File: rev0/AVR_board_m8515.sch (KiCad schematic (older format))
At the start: 8 parts

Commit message: added all needed labels and stuff
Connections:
- net VCC: now also P?.1 (P1)
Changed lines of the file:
@@
 LIBS:contrib
 LIBS:valves
+LIBS:AVR_board_m8515-cache
 EELAYER 24 0
 EELAYER END
@@
 Wire Wire Line
 	7350 3850 7350 3950
+$Comp
+L VCC #PWR?
+U 1 1 54189251
+P 6600 800
+F 0 "#PWR?" H 6600 900 30  0001 C CNN
+F 1 "VCC" H 6600 900 30  0000 C CNN
+F 2 "" H 6600 800 60  0000 C CNN
+F 3 "" H 6600 800 60  0000 C CNN
+	1    6600 800
+	1    0    0    -1
+$EndComp
+Wire Wire Line
+	6600 800  6600 1000
+Wire Wire Line
+	6600 1000 6700 1000
+Text GLabel 6500 1100 0    60   Input ~ 0
+PA0
+Text GLabel 6500 1200 0    60   Input ~ 0
+PA1
+Text GLabel 6500 1300 0    60   Input ~ 0
+PA2
+Text GLabel 6500 1400 0    60   Input ~ 0
+PA3
+Text GLabel 6500 1500 0    60   Input ~ 0
+PA4
+Text GLabel 6500 1600 0    60   Input ~ 0
+PA5
+Text GLabel 6500 1700 0    60   Input ~ 0
+PA6
+Text GLabel 6500 1800 0    60   Input ~ 0
+PA7
+Text GLabel 6500 1900 0    60   Input ~ 0
+PE0
+Text GLabel 6500 2000 0    60   Input ~ 0
+PE1
+Text GLabel 6500 2100 0    60   Input ~ 0
+PE2
+Text GLabel 6500 2200 0    60   Input ~ 0
+PC7
+Text GLabel 6500 2300 0    60   Input ~ 0
+PC6
+Text GLabel 6500 2400 0    60   Input ~ 0
+PC5
+Text GLabel 6500 2500 0    60   Input ~ 0
+PC4
+Text GLabel 6500 2600 0    60   Input ~ 0
+PC3
+Text GLabel 6500 2700 0    60   Input ~ 0
+PC2
+Text GLabel 6500 2800 0    60   Input ~ 0
+PC1
+Text GLabel 6500 2900 0    60   Input ~ 0
+PC0
+Text GLabel 3800 1000 2    60   Input ~ 0
+PB0
+Text GLabel 3800 1100 2    60   Input ~ 0
+PB1
+Text GLabel 3800 1200 2    60   Input ~ 0
+PB2
+Text GLabel 3800 1300 2    60   Input ~ 0
+PB3
+Text GLabel 3800 1400 2    60   Input ~ 0
+PB4
+Text GLabel 3800 1500 2    60   Input ~ 0
+PB5
+Text GLabel 3800 1600 2    60   Input ~ 0
+PB6
+Text GLabel 3800 1700 2    60   Input ~ 0
+PB7
+Text GLabel 3800 1800 2    60   Input ~ 0
+RESET
+Text GLabel 3800 1900 2    60   Input ~ 0
+PD0
+Text GLabel 3800 2000 2    60   Input ~ 0
+PD1
+Text GLabel 3800 2100 2    60   Input ~ 0
+PD2
+Text GLabel 3800 2200 2    60   Input ~ 0
+PD3
+Text GLabel 3800 2300 2    60   Input ~ 0
+PD4
+Text GLabel 3800 2400 2    60   Input ~ 0
+PD5
+Text GLabel 3800 2500 2    60   Input ~ 0
+PD6
+Text GLabel 3800 2600 2    60   Input ~ 0
+PD7
+Text GLabel 3800 2700 2    60   Input ~ 0
+XTAL2
+Text GLabel 3800 2800 2    60   Input ~ 0
+XTAL1
+Text GLabel 3800 2900 2    60   Input ~ 0
+GND
 $EndSCHEMATC

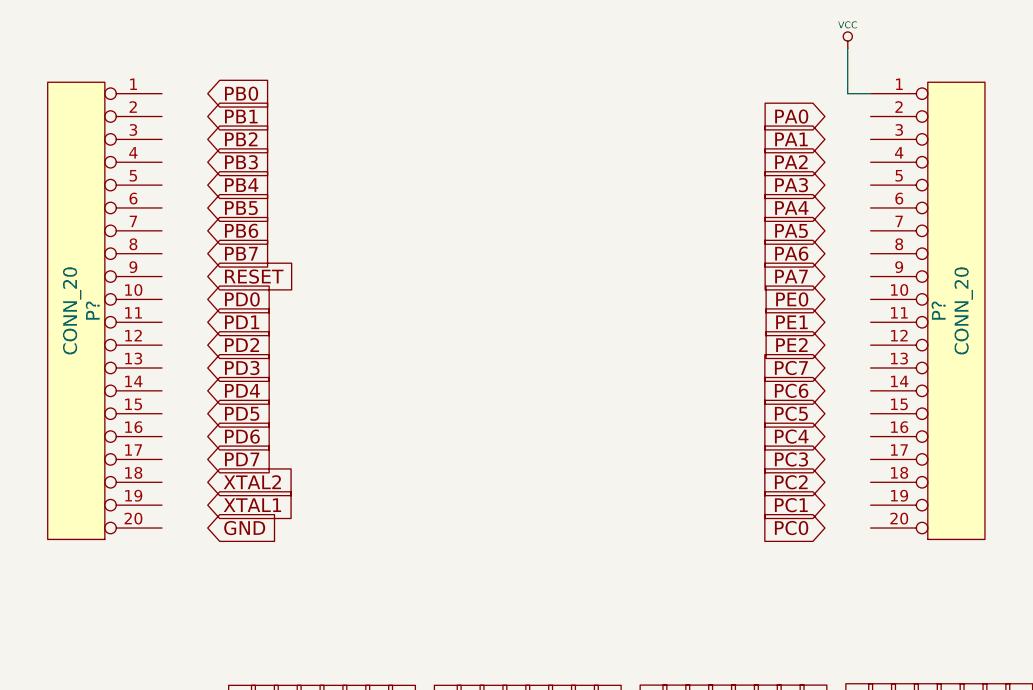
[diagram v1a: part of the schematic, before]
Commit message: added connections to the labels
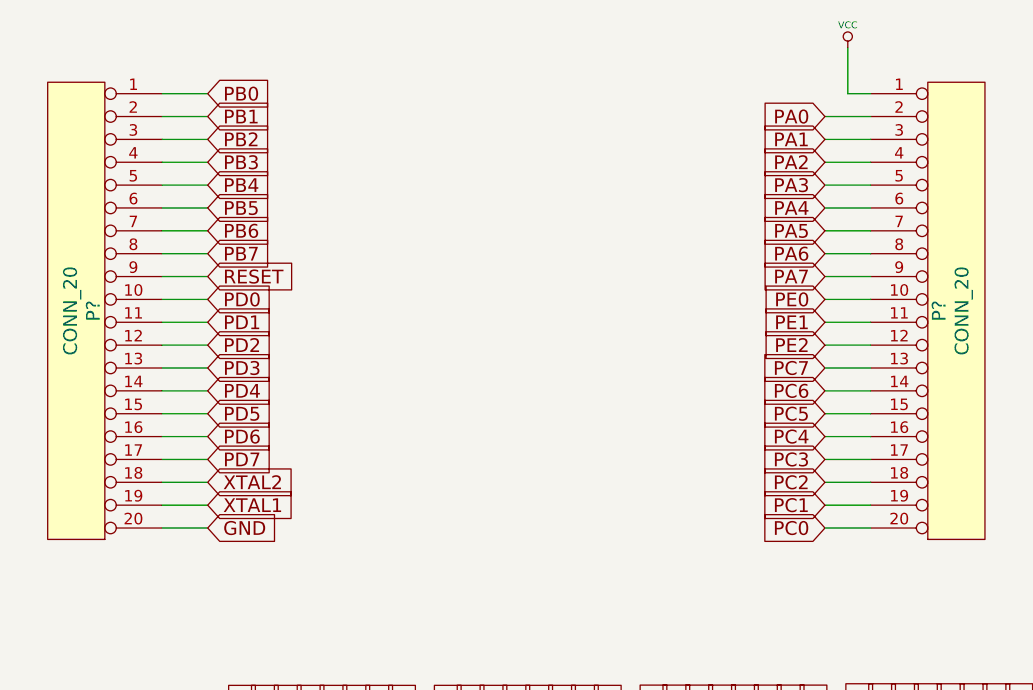
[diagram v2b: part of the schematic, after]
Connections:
- net GND: now also P?.20 (P20)
- net PA0: now also P?.2 (P2)
- net PA1: now also P?.3 (P3)
- net PA2: now also P?.4 (P4)
- net PA3: now also P?.5 (P5)
- net PA4: now also P?.6 (P6)
- net PA5: now also P?.7 (P7)
- net PA6: now also P?.8 (P8)
- net PA7: now also P?.9 (P9)
- net PB0: now also P?.1 (P1)
- net PB1: now also P?.2 (P2)
- net PB2: now also P?.3 (P3)
- net PB3: now also P?.4 (P4)
- net PB4: now also P?.5 (P5)
- net PB5: now also P?.6 (P6)
- net PB6: now also P?.7 (P7)
- net PB7: now also P?.8 (P8)
- net PC0: now also P?.20 (P20)
- net PC1: now also P?.19 (P19)
- net PC2: now also P?.18 (P18)
- net PC3: now also P?.17 (P17)
- net PC4: now also P?.16 (P16)
- net PC5: now also P?.15 (P15)
- net PC6: now also P?.14 (P14)
- net PC7: now also P?.13 (P13)
- net PD0: now also P?.10 (P10)
- net PD1: now also P?.11 (P11)
- net PD2: now also P?.12 (P12)
- net PD3: now also P?.13 (P13)
- net PD4: now also P?.14 (P14)
- net PD5: now also P?.15 (P15)
- net PD6: now also P?.16 (P16)
- net PD7: now also P?.17 (P17)
- net PE0: now also P?.10 (P10)
- net PE1: now also P?.11 (P11)
- net PE2: now also P?.12 (P12)
- net RESET: now also P?.9 (P9)
- net XTAL1: now also P?.19 (P19)
- net XTAL2: now also P?.18 (P18)
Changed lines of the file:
@@
 Text GLabel 3800 2900 2    60   Input ~ 0
 GND
+Wire Wire Line
+	3800 1000 3600 1000
+Wire Wire Line
+	3800 1100 3600 1100
+Wire Wire Line
+	3800 1200 3600 1200
+Wire Wire Line
+	3800 1300 3600 1300
+Wire Wire Line
+	3800 1400 3600 1400
+Wire Wire Line
+	3800 1500 3600 1500
+Wire Wire Line
+	3800 1600 3600 1600
+Wire Wire Line
+	3800 1700 3600 1700
+Wire Wire Line
+	3800 1800 3600 1800
+Wire Wire Line
+	3800 1900 3600 1900
+Wire Wire Line
+	3800 2000 3600 2000
+Wire Wire Line
+	3800 2100 3600 2100
+Wire Wire Line
+	3800 2200 3600 2200
+Wire Wire Line
+	3800 2300 3600 2300
+Wire Wire Line
+	3600 2400 3800 2400
+Wire Wire Line
+	3800 2500 3600 2500
+Wire Wire Line
+	3800 2600 3600 2600
+Wire Wire Line
+	3800 2700 3600 2700
+Wire Wire Line
+	3800 2800 3600 2800
+Wire Wire Line
+	3800 2900 3600 2900
+Wire Wire Line
+	6500 1100 6700 1100
+Wire Wire Line
+	6700 1200 6500 1200
+Wire Wire Line
+	6500 1300 6700 1300
+Wire Wire Line
+	6700 1400 6500 1400
+Wire Wire Line
+	6700 1500 6500 1500
+Wire Wire Line
+	6700 1600 6500 1600
+Wire Wire Line
+	6700 1700 6500 1700
+Wire Wire Line
+	6700 1800 6500 1800
+Wire Wire Line
+	6700 1900 6500 1900
+Wire Wire Line
+	6700 2000 6500 2000
+Wire Wire Line
+	6700 2100 6500 2100
+Wire Wire Line
+	6700 2200 6500 2200
+Wire Wire Line
+	6700 2300 6500 2300
+Wire Wire Line
+	6700 2400 6500 2400
+Wire Wire Line
+	6700 2500 6500 2500
+Wire Wire Line
+	6700 2600 6500 2600
+Wire Wire Line
+	6500 2700 6700 2700
+Wire Wire Line
+	6700 2800 6500 2800
+Wire Wire Line
+	6500 2900 6700 2900
 $EndSCHEMATC

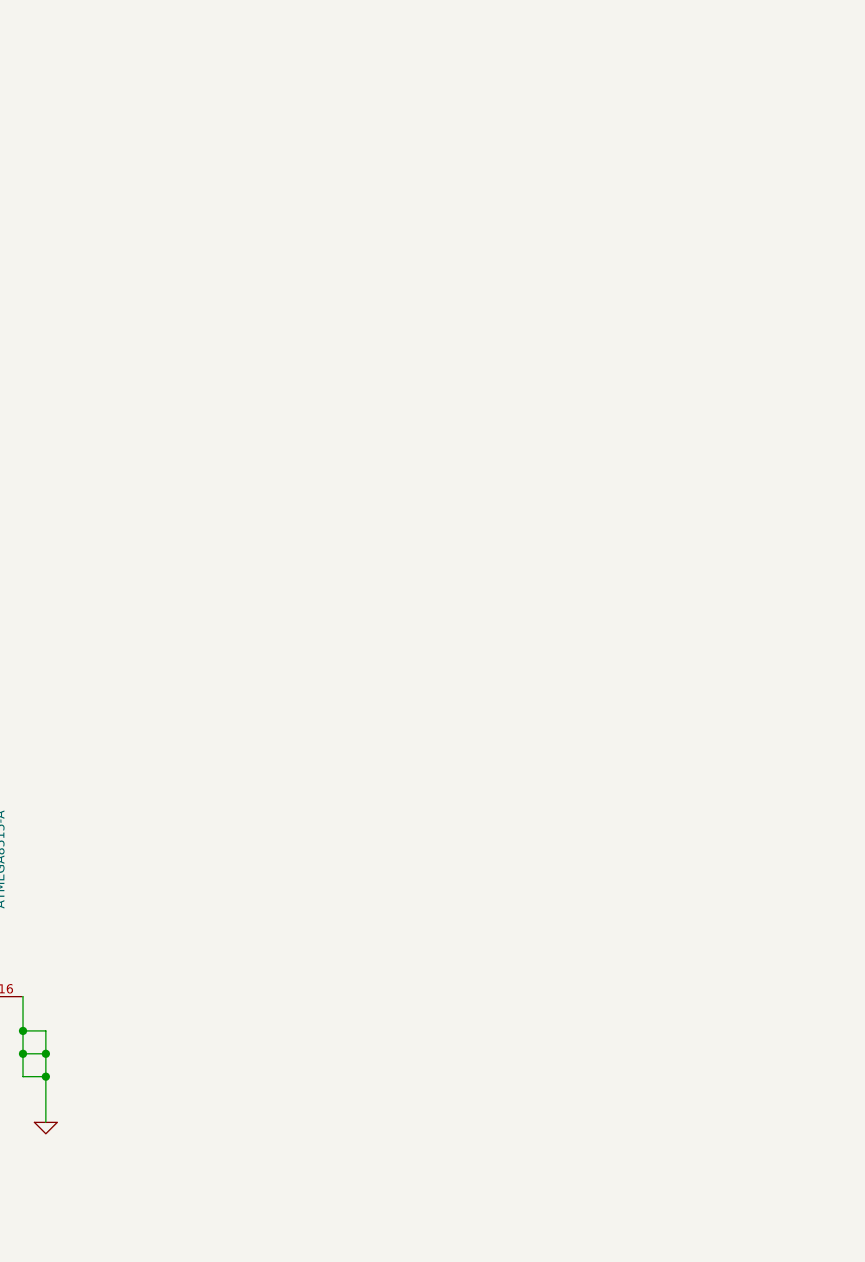
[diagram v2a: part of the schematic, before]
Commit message: added wires to the things to other mcu pad placeholder thingy
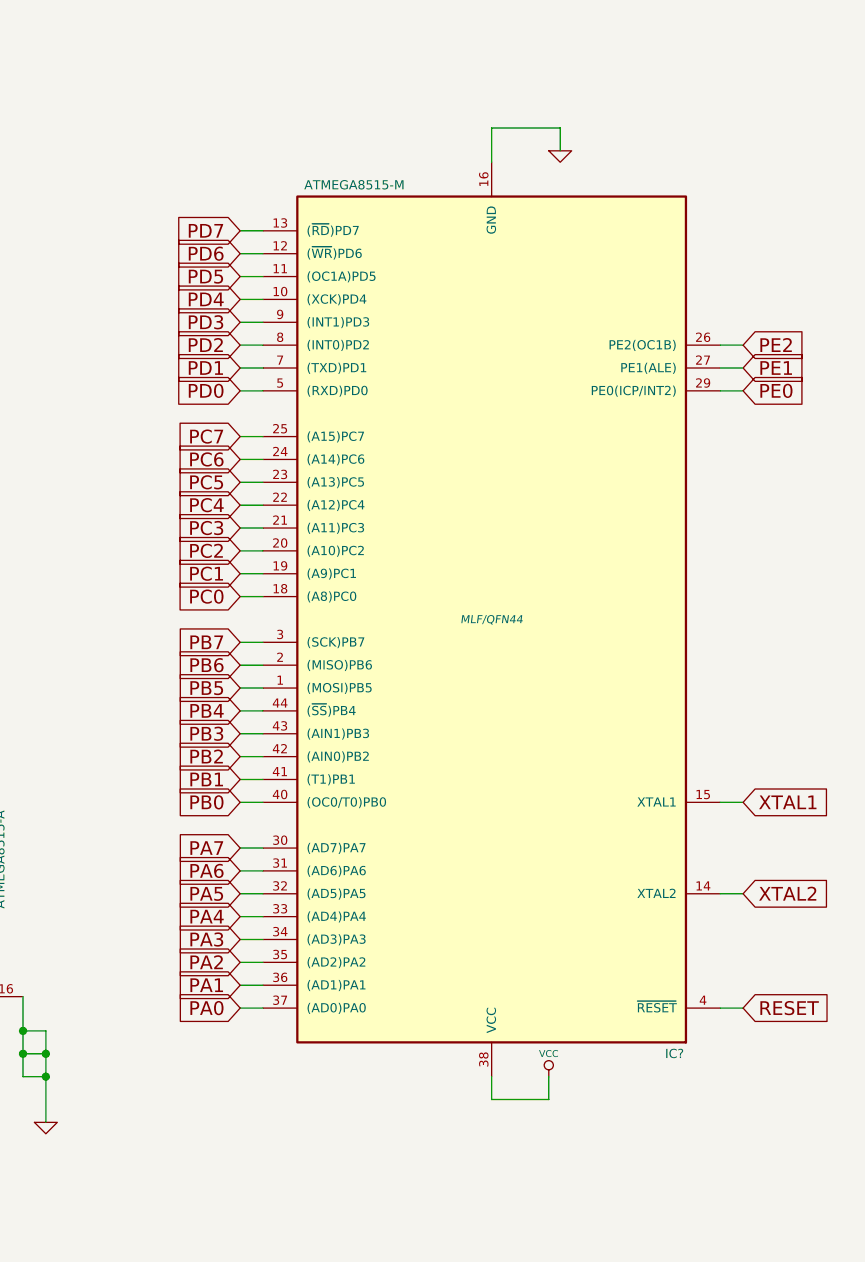
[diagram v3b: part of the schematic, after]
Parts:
- added IC?: ATMEGA8515-M, MLF/QFN44, symbol ATMEGA8515-M
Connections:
- net GND: now also IC?.16 (GND)
- net PA0: now also IC?.37 ((AD0)PA0)
- net PA1: now also IC?.36 ((AD1)PA1)
- net PA2: now also IC?.35 ((AD2)PA2)
- net PA3: now also IC?.34 ((AD3)PA3)
- net PA4: now also IC?.33 ((AD4)PA4)
- net PA5: now also IC?.32 ((AD5)PA5)
- net PA6: now also IC?.31 ((AD6)PA6)
- net PA7: now also IC?.30 ((AD7)PA7)
- net PB0: now also IC?.40 ((OC0/T0)PB0)
- net PB1: now also IC?.41 ((T1)PB1)
- net PB2: now also IC?.42 ((AIN0)PB2)
- net PB3: now also IC?.43 ((AIN1)PB3)
- net PB4: now also IC?.44 ((~SS~)PB4)
- net PB5: now also IC?.1 ((MOSI)PB5)
- net PB6: now also IC?.2 ((MISO)PB6)
- net PB7: now also IC?.3 ((SCK)PB7)
- net PC0: now also IC?.18 ((A8)PC0)
- net PC1: now also IC?.19 ((A9)PC1)
- net PC2: now also IC?.20 ((A10)PC2)
- net PC3: now also IC?.21 ((A11)PC3)
- net PC4: now also IC?.22 ((A12)PC4)
- net PC5: now also IC?.23 ((A13)PC5)
- net PC6: now also IC?.24 ((A14)PC6)
- net PC7: now also IC?.25 ((A15)PC7)
- net PD0: now also IC?.5 ((RXD)PD0)
- net PD1: now also IC?.7 ((TXD)PD1)
- net PD2: now also IC?.8 ((INT0)PD2)
- net PD3: now also IC?.9 ((INT1)PD3)
- net PD4: now also IC?.10 ((XCK)PD4)
- net PD5: now also IC?.11 ((OC1A)PD5)
- net PD6: now also IC?.12 ((~WR~)PD6)
- net PD7: now also IC?.13 ((~RD~)PD7)
- net PE0: now also IC?.29 (PE0(ICP/INT2))
- net PE1: now also IC?.27 (PE1(ALE))
- net PE2: now also IC?.26 (PE2(OC1B))
- net RESET: now also IC?.4 (~RESET)
- net VCC: now also IC?.38 (VCC)
- net XTAL1: now also IC?.15 (XTAL1)
- net XTAL2: now also IC?.14 (XTAL2)
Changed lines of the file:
@@
 Wire Wire Line
 	6500 2900 6700 2900
+$Comp
+L ATMEGA8515-M IC?
+U 1 1 5418A671
+P 9700 3300
+F 0 "IC?" H 8900 5200 40  0000 C CNN
+F 1 "ATMEGA8515-M" H 10300 1400 40  0000 C CNN
+F 2 "MLF/QFN44" H 9700 3300 35  0000 C CIN
+F 3 "" H 9700 3300 60  0000 C CNN
+	1    9700 3300
+	-1   0    0    1
+$EndComp
+$Comp
+L GND #PWR?
+U 1 1 5418A680
+P 10000 1250
+F 0 "#PWR?" H 10000 1250 30  0001 C CNN
+F 1 "GND" H 10000 1180 30  0001 C CNN
+F 2 "" H 10000 1250 60  0000 C CNN
+F 3 "" H 10000 1250 60  0000 C CNN
+	1    10000 1250
+	1    0    0    -1
+$EndComp
+Wire Wire Line
+	9700 1300 9700 1150
+Wire Wire Line
+	9700 1150 10000 1150
+Wire Wire Line
+	10000 1150 10000 1250
+Text GLabel 8600 1600 0    60   Input ~ 0
+PD7
+Text GLabel 8600 1700 0    60   Input ~ 0
+PD6
+Text GLabel 8600 1800 0    60   Input ~ 0
+PD5
+Text GLabel 8600 1900 0    60   Input ~ 0
+PD4
+Text GLabel 8600 2000 0    60   Input ~ 0
+PD3
+Text GLabel 8600 2100 0    60   Input ~ 0
+PD2
+Text GLabel 8600 2200 0    60   Input ~ 0
+PD1
+Text GLabel 8600 2300 0    60   Input ~ 0
+PD0
+Text GLabel 8600 2500 0    60   Input ~ 0
+PC7
+Text GLabel 8600 2600 0    60   Input ~ 0
+PC6
+Text GLabel 8600 2700 0    60   Input ~ 0
+PC5
+Text GLabel 8600 2800 0    60   Input ~ 0
+PC4
+Text GLabel 8600 2900 0    60   Input ~ 0
+PC3
+Text GLabel 8600 3000 0    60   Input ~ 0
+PC2
+Text GLabel 8600 3100 0    60   Input ~ 0
+PC1
+Text GLabel 8600 3200 0    60   Input ~ 0
+PC0
+Text GLabel 8600 3400 0    60   Input ~ 0
+PB7
+Text GLabel 8600 3500 0    60   Input ~ 0
+PB6
+Text GLabel 8600 3600 0    60   Input ~ 0
+PB5
+Text GLabel 8600 3700 0    60   Input ~ 0
+PB4
+Text GLabel 8600 3800 0    60   Input ~ 0
+PB3
+Text GLabel 8600 3900 0    60   Input ~ 0
+PB2
+Text GLabel 8600 4000 0    60   Input ~ 0
+PB1
+Text GLabel 8600 4100 0    60   Input ~ 0
+PB0
+Text GLabel 8600 4300 0    60   Input ~ 0
+PA7
+Text GLabel 8600 4400 0    60   Input ~ 0
+PA6
+Text GLabel 8600 4500 0    60   Input ~ 0
+PA5
+Text GLabel 8600 4600 0    60   Input ~ 0
+PA4
+Text GLabel 8600 4700 0    60   Input ~ 0
+PA3
+Text GLabel 8600 4800 0    60   Input ~ 0
+PA2
+Text GLabel 8600 4900 0    60   Input ~ 0
+PA1
+Text GLabel 8600 5000 0    60   Input ~ 0
+PA0
+$Comp
+L VCC #PWR?
+U 1 1 5418A7C7
+P 9950 5300
+F 0 "#PWR?" H 9950 5400 30  0001 C CNN
+F 1 "VCC" H 9950 5400 30  0000 C CNN
+F 2 "" H 9950 5300 60  0000 C CNN
+F 3 "" H 9950 5300 60  0000 C CNN
+	1    9950 5300
+	1    0    0    -1
+$EndComp
+Wire Wire Line
+	9700 5300 9700 5400
+Wire Wire Line
+	9700 5400 9950 5400
+Wire Wire Line
+	9950 5400 9950 5300
+Text GLabel 10800 5000 2    60   Input ~ 0
+RESET
+Text GLabel 10800 4500 2    60   Input ~ 0
+XTAL2
+Text GLabel 10800 4100 2    60   Input ~ 0
+XTAL1
+Text GLabel 10800 2300 2    60   Input ~ 0
+PE0
+Text GLabel 10800 2200 2    60   Input ~ 0
+PE1
+Text GLabel 10800 2100 2    60   Input ~ 0
+PE2
+Wire Wire Line
+	10800 4100 10700 4100
+Wire Wire Line
+	10800 4500 10700 4500
+Wire Wire Line
+	10800 5000 10700 5000
+Wire Wire Line
+	10800 2100 10700 2100
+Wire Wire Line
+	10800 2200 10700 2200
+Wire Wire Line
+	10800 2300 10700 2300
+Wire Wire Line
+	8600 1600 8700 1600
+Wire Wire Line
+	8600 1700 8700 1700
+Wire Wire Line
+	8700 1800 8600 1800
+Wire Wire Line
+	8600 1900 8700 1900
+Wire Wire Line
+	8700 2000 8600 2000
+Wire Wire Line
+	8700 2100 8600 2100
+Wire Wire Line
+	8700 2200 8600 2200
+Wire Wire Line
+	8700 2300 8600 2300
+Wire Wire Line
+	8700 2500 8600 2500
+Wire Wire Line
+	8700 2600 8600 2600
+Wire Wire Line
+	8700 2700 8600 2700
+Wire Wire Line
+	8700 2800 8600 2800
+Wire Wire Line
+	8700 2900 8600 2900
+Wire Wire Line
+	8700 3000 8600 3000
+Wire Wire Line
+	8700 3100 8600 3100
+Wire Wire Line
+	8700 3200 8600 3200
+Wire Wire Line
+	8700 3400 8600 3400
+Wire Wire Line
+	8700 3500 8600 3500
+Wire Wire Line
+	8700 3600 8600 3600
+Wire Wire Line
+	8700 3700 8600 3700
+Wire Wire Line
+	8700 3800 8600 3800
+Wire Wire Line
+	8700 3900 8600 3900
+Wire Wire Line
+	8700 4000 8600 4000
+Wire Wire Line
+	8700 4100 8600 4100
+Wire Wire Line
+	8700 4300 8600 4300
+Wire Wire Line
+	8700 4400 8600 4400
+Wire Wire Line
+	8700 4500 8600 4500
+Wire Wire Line
+	8700 4600 8600 4600
+Wire Wire Line
+	8700 4700 8600 4700
+Wire Wire Line
+	8700 4800 8600 4800
+Wire Wire Line
+	8700 4900 8600 4900
+Wire Wire Line
+	8700 5000 8600 5000
 $EndSCHEMATC

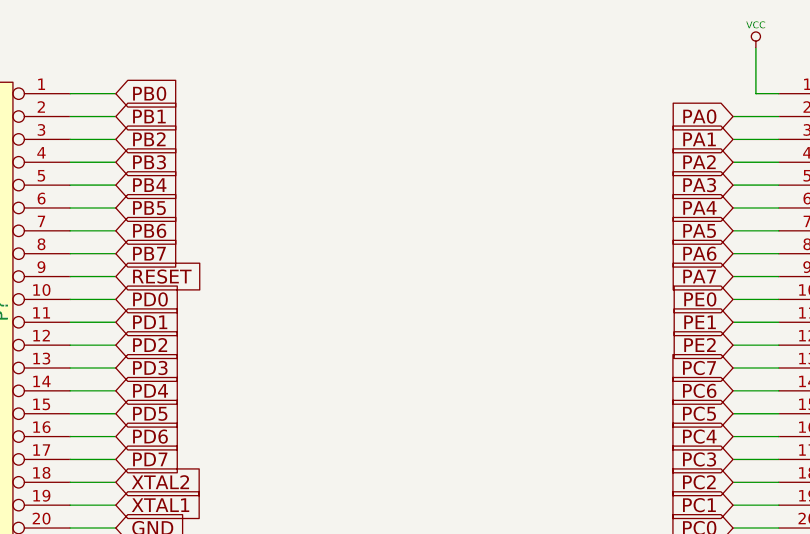
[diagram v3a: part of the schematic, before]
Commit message: added isp conn to schematic
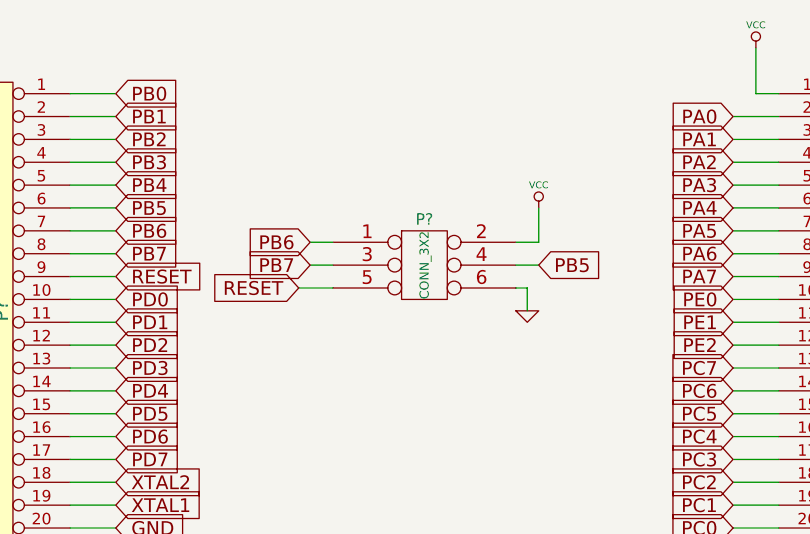
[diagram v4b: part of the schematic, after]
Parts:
- added P?: CONN_3X2, symbol CONN_3X2
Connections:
- net GND: now also P?.6
- net PB5: now also P?.4
- net PB6: now also P?.1
- net PB7: now also P?.3
- net RESET: now also P?.5
- net VCC: now also P?.2
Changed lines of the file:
@@
 Wire Wire Line
 	8700 5000 8600 5000
+$Comp
+L CONN_3X2 P?
+U 1 1 5418C01F
+P 5150 1800
+F 0 "P?" H 5150 2050 50  0000 C CNN
+F 1 "CONN_3X2" V 5150 1850 40  0000 C CNN
+F 2 "" H 5150 1800 60  0000 C CNN
+F 3 "" H 5150 1800 60  0000 C CNN
+	1    5150 1800
+	1    0    0    -1
+$EndComp
+$Comp
+L VCC #PWR?
+U 1 1 5418C02E
+P 5650 1500
+F 0 "#PWR?" H 5650 1600 30  0001 C CNN
+F 1 "VCC" H 5650 1600 30  0000 C CNN
+F 2 "" H 5650 1500 60  0000 C CNN
+F 3 "" H 5650 1500 60  0000 C CNN
+	1    5650 1500
+	1    0    0    -1
+$EndComp
+Wire Wire Line
+	5650 1500 5650 1650
+Wire Wire Line
+	5650 1650 5550 1650
+Text GLabel 5650 1750 2    60   Input ~ 0
+PB5
+$Comp
+L GND #PWR?
+U 1 1 5418C0DE
+P 5600 1950
+F 0 "#PWR?" H 5600 1950 30  0001 C CNN
+F 1 "GND" H 5600 1880 30  0001 C CNN
+F 2 "" H 5600 1950 60  0000 C CNN
+F 3 "" H 5600 1950 60  0000 C CNN
+	1    5600 1950
+	1    0    0    -1
+$EndComp
+Wire Wire Line
+	5550 1850 5600 1850
+Wire Wire Line
+	5600 1850 5600 1950
+Wire Wire Line
+	5650 1750 5550 1750
+Text GLabel 4650 1650 0    60   Input ~ 0
+PB6
+Text GLabel 4650 1750 0    60   Input ~ 0
+PB7
+Text GLabel 4600 1850 0    60   Input ~ 0
+RESET
+Wire Wire Line
+	4650 1650 4750 1650
+Wire Wire Line
+	4750 1750 4650 1750
+Wire Wire Line
+	4750 1850 4600 1850
 $EndSCHEMATC
